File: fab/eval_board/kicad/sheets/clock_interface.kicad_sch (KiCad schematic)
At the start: 17 parts, among them J10 SMA_RF4, J2 USB-C, J5 JTAG_2x5, J6 GPIO_2x7, J7 SMA_RF1, J8 SMA_RF2, J9 SMA_RF3, SW1 RESET, U20 Si5395A, U22 FT232H, U23 W25Q128JVS, Y1 100MHz_TCXO

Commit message: fix: regenerate KiCad files in valid KiCad 8 format
- Rewrote all .kicad_sch files with proper lib_symbols sections,
  symbol instances, wires, hierarchical sheet references, and
  power port definitions (removed invalid ';;' comment syntax)
- Fixed .kicad_pcb: removed comment lines, added 922 missing net
  definitions, fixed gr_text justify format
- Regenerated Gerbers from fixed PCB using kicad-cli (30 files)
- All files validated with kicad-cli: schematic exports 5-page PDF,
  PCB exports SVG, DRC/ERC both run without parse errors
- Added regenerate_kicad.py generator script for reproducibility

Co-Authored-By: Bola Olatunji <bola.olatunji@ai.lightos.sh>
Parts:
- removed D1: LED_Green_PWR, LED_SMD:LED_0603_1608Metric, symbol Device:LED
- removed D2: LED_Blue_ACT, LED_SMD:LED_0603_1608Metric, symbol Device:LED
- removed D3: LED_Red_FAULT, LED_SMD:LED_0603_1608Metric, symbol Device:LED
- removed D4: LED_Yellow_LINK, LED_SMD:LED_0603_1608Metric, symbol Device:LED
- removed D5: PRTR5V0U2X, Package_TO_SOT_SMD:SOD-323, symbol Diode:PRTR5V0U2X
- removed J10: SMA_RF4, Connector_Coaxial:SMA_Amphenol_132134-11_Vertical, symbol Connector:Conn_Coaxial
- removed J2: USB-C, Connector_USB:USB_C_Receptacle_GCT_USB4110-GF-A, symbol Connector:USB_C_Receptacle_USB2.0
- removed J5: JTAG_2x5, Connector_PinHeader_1.27mm:PinHeader_2x05_P1.27mm_Vertical, symbol Connector:Conn_ARM_JTAG_SWD_10
- removed J6: GPIO_2x7, Connector_PinHeader_1.27mm:PinHeader_2x07_P1.27mm_Vertical, symbol Connector_Generic:Conn_02x07_Odd_Even
- removed J7: SMA_RF1, Connector_Coaxial:SMA_Amphenol_132134-11_Vertical, symbol Connector:Conn_Coaxial
- removed J8: SMA_RF2, Connector_Coaxial:SMA_Amphenol_132134-11_Vertical, symbol Connector:Conn_Coaxial
- removed J9: SMA_RF3, Connector_Coaxial:SMA_Amphenol_132134-11_Vertical, symbol Connector:Conn_Coaxial
- removed U23: W25Q128JVS, Package_SON:WSON-8-1EP_2x3mm_P0.5mm, symbol Memory_Flash:W25Q128JVS
- removed Y1: 100MHz_TCXO, Oscillator:Oscillator_SMD_3225-4Pin_3.2x2.5mm, symbol Oscillator:SiT5356
- added C50, C51, C52, C53: 100nF, Capacitor_SMD:C_0402_1005Metric, symbol Device:C
- added J2: USB_C, Connector_USB:USB_C_Receptacle_GCT_USB4105-xx-A_16P_TopMnt_Horizontal, symbol Connector:USB_C_Receptacle
- added J6: GPIO_2x7, Connector_PinHeader_2.54mm:PinHeader_2x07_P2.54mm_Vertical, symbol Connector_Generic:Conn_02x07
- added Y1: 100MHz_TCXO, Crystal:Crystal_SMD_2520-4Pin_2.5x2.0mm, symbol Device:Crystal
- SW1: footprint Button_Switch_SMD:SW_Push_1P1T_NO_CK_KSC701J -> Button_Switch_SMD:SW_Push_1P1T_NO_CK_KSC7xxJ; MPN B3F-1000 -> KSC721J
- U20: footprint LightRail:QFN-28_5x5mm -> Package_DFN_QFN:QFN-44-1EP_7x7mm_P0.5mm_EP5.15x5.15mm; MPN Si5395A-A-GM -> SI5395A-A-GM
- U22: value FT232H -> FT232HL; footprint Package_DFN_QFN:QFN-48-1EP_7x7mm_P0.5mm_EP5.15x5.15mm -> Package_QFP:LQFP-48_7x7mm_P0.5mm; MPN FT232HQ -> FT232HL-REEL
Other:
- title: Clock & Test Interface — LightRail Eval Board -> Clock Generation + Test Interface - LightRail Eval Board

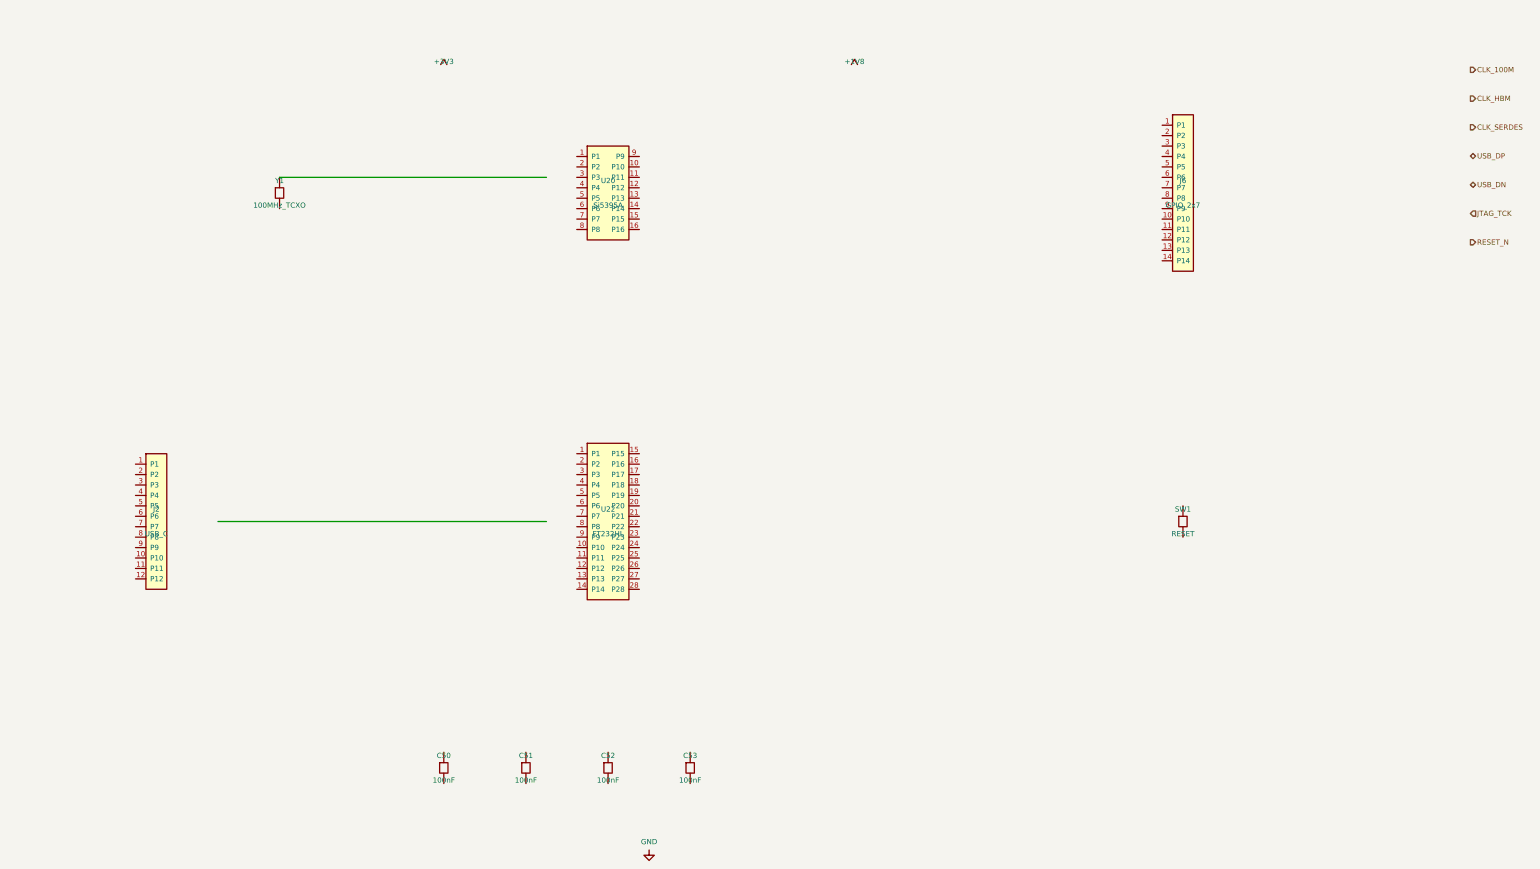
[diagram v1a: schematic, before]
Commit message: refactor: improve ERC quality via grid snapping and power flags
Co-Authored-By: Bola Olatunji <bola.olatunji@ai.lightos.sh>
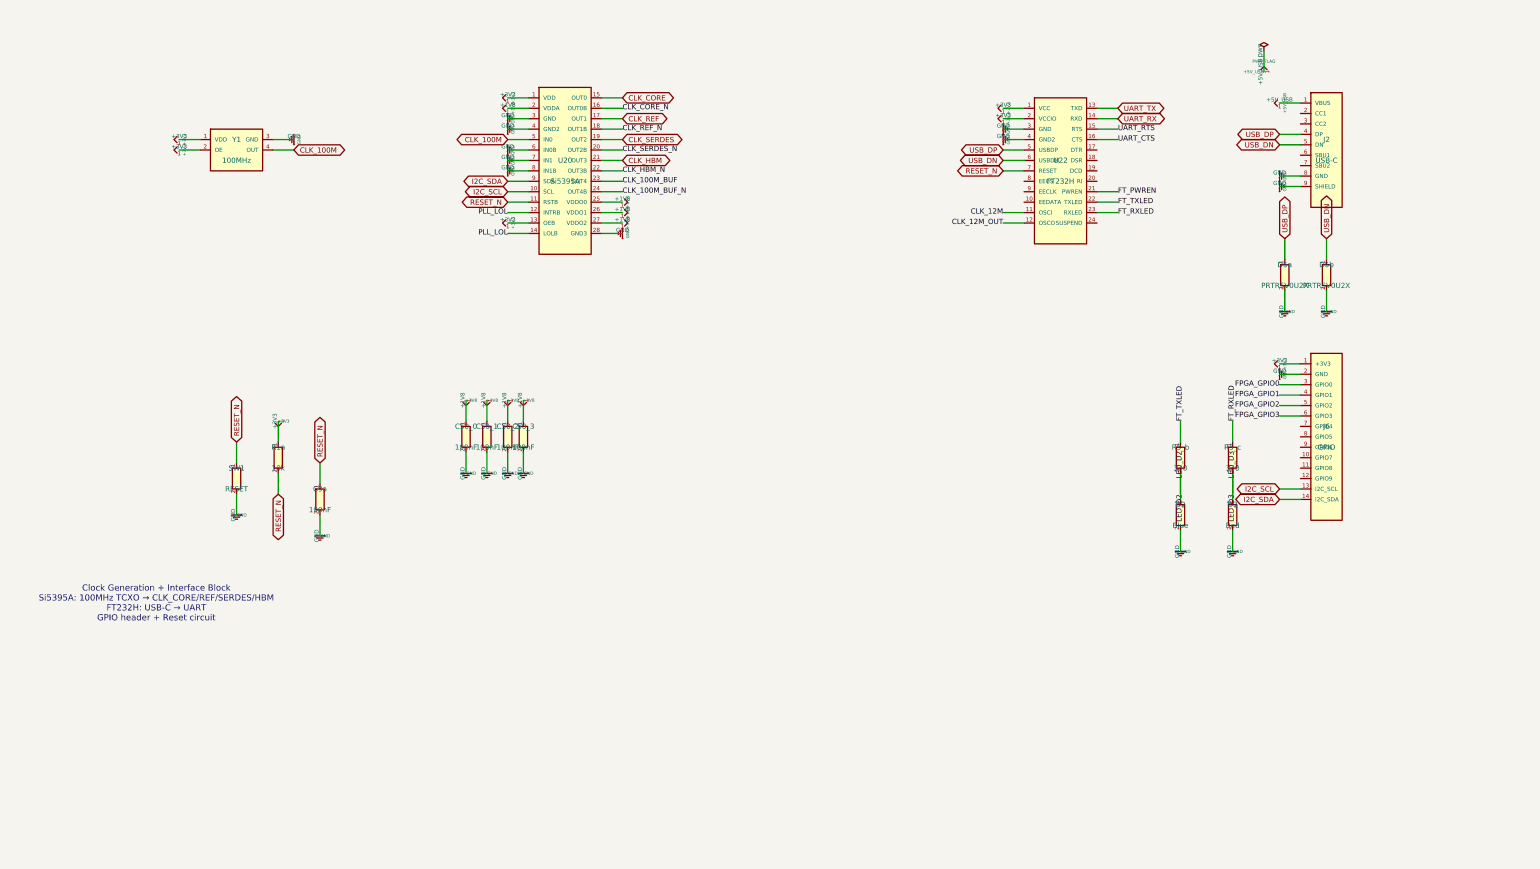
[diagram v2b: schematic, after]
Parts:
- removed C50, C51, C52, C53: 100nF, Capacitor_SMD:C_0402_1005Metric, symbol Device:C
- removed J2: USB_C, Connector_USB:USB_C_Receptacle_GCT_USB4105-xx-A_16P_TopMnt_Horizontal, symbol Connector:USB_C_Receptacle
- removed J6: GPIO_2x7, Connector_PinHeader_2.54mm:PinHeader_2x07_P2.54mm_Vertical, symbol Connector_Generic:Conn_02x07
- removed Y1: 100MHz_TCXO, Crystal:Crystal_SMD_2520-4Pin_2.5x2.0mm, symbol Device:Crystal
- added C50_0, C50_1, C50_2, C50_3: 100nF, symbol Device:C
- added C9a: 100nF, Capacitor_SMD:C_0402, symbol Device:C
- added D2: Blue, LED_SMD:LED_0603, symbol Device:LED
- added D3: Red, LED_SMD:LED_0603, symbol Device:LED
- added D5a, D5b: PRTR5V0U2X, Package_SOD:SOD-323, symbol Device:D_TVS
- added J2: USB-C, Connector_USB:USB_C_Receptacle_GCT_USB4110, symbol Connector:USB_C_16Pin
- added J6: GPIO, Connector_PinHeader_1.27mm:PinHeader_2x07_P1.27mm_Vertical, symbol Connector:PinHeader_2x07
- added R1a: 10k, Resistor_SMD:R_0402, symbol Device:R
- added R5_b, R5_c: 330, Resistor_SMD:R_0402, symbol Device:R
- added Y1: 100MHz, Crystal:Crystal_SMD_3215-4Pin, symbol Device:Crystal_4Pin
- SW1: footprint Button_Switch_SMD:SW_Push_1P1T_NO_CK_KSC7xxJ -> Button_Switch_SMD:Tactile_4.5x4.5mm; MPN KSC721J -> B3F-1000
- U20: footprint Package_DFN_QFN:QFN-44-1EP_7x7mm_P0.5mm_EP5.15x5.15mm -> Package_DFN_QFN:QFN-28_5x5mm; MPN SI5395A-A-GM -> Si5395A-A-GM
- U22: value FT232HL -> FT232H; footprint Package_QFP:LQFP-48_7x7mm_P0.5mm -> Package_DFN_QFN:QFN-48_7x7mm; MPN FT232HL-REEL -> FT232HQ
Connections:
- net +1V8: now also U20.2 (VDDA), U20.25 (VDDO0), U20.26 (VDDO1), U20.27 (VDDO2), C50_0.1, C50_1.1, C50_2.1, C50_3.1
- net +3V3: now also U20.1 (VDD), U20.13 (OEB), U22.1 (VCC), U22.2 (VCCIO), J6.1 (+3V3), R1a.1, Y1.1 (VDD), Y1.2 (OE)
- net CLK_100M: now also U20.5 (IN0), Y1.4 (OUT)
- net CLK_HBM: now also U20.21 (OUT3)
- net CLK_SERDES: now also U20.19 (OUT2)
- net GND: now also SW1.2, U20.28 (GND3), U20.3 (GND), U20.4 (GND2), U20.6 (IN0B), U20.7 (IN1), U20.8 (IN1B), U22.3 (GND), U22.4 (GND2), C50_0.2, C50_1.2, C50_2.2, C50_3.2, C9a.2, D2.2, D3.2, D5a.2, D5b.2, J2.8 (GND), J2.9 (SHIELD), J6.2 (GND), Y1.3 (GND)
- net RESET_N: now also SW1.1, U20.11 (RSTB), U22.7 (RESET), C9a.1, R1a.2
- net USB_DN: now also U22.6 (USBDM), D5b.1, J2.5 (DN)
- net USB_DP: now also U22.5 (USBDP), D5a.1, J2.4 (DP)
- net CLK_12M: now reaches U22.11 (OSCI)
- net CLK_12M_OUT: now reaches U22.12 (OSCO)
- net UART_TX: now reaches U22.13 (TXD)
- net UART_RX: now reaches U22.14 (RXD)
- net UART_RTS: now reaches U22.15 (RTS)
- net UART_CTS: now reaches U22.16 (CTS)
- net FT_PWREN: now reaches U22.21 (PWREN)
- net FT_TXLED: now reaches U22.22 (TXLED)
- net FT_TXLED: now also R5_b.1
- net FT_RXLED: now reaches U22.23 (RXLED)
- net FT_RXLED: now also R5_c.1
- net I2C_SCL: now reaches U20.10 (SCL)
- net I2C_SCL: now also J6.13 (I2C_SCL)
- net PLL_LOL: now reaches U20.12 (INTRB)
- net PLL_LOL: now also U20.14 (LOLB)
- net CLK_CORE: now reaches U20.15 (OUT0)
- net CLK_CORE_N: now reaches U20.16 (OUT0B)
- net I2C_SDA: now reaches U20.9 (SDA)
- net I2C_SDA: now also J6.14 (I2C_SDA)
- new net +5V_USB: J2.1 (VBUS)
- new net CLK_100M_BUF: U20.23 (OUT4)
- new net CLK_100M_BUF_N: U20.24 (OUT4B)
- new net CLK_HBM_N: U20.22 (OUT3B)
- new net CLK_REF: U20.17 (OUT1)
- new net CLK_REF_N: U20.18 (OUT1B)
- new net CLK_SERDES_N: U20.20 (OUT2B)
- new net FPGA_GPIO0: J6.3 (GPIO0)
- new net FPGA_GPIO1: J6.4 (GPIO1)
- new net FPGA_GPIO2: J6.5 (GPIO2)
- new net FPGA_GPIO3: J6.6 (GPIO3)
- new net LED_D2: D2.1, R5_b.2
- new net LED_D3: D3.1, R5_c.2
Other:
- note added: "Clock Generation + Interface Block Si5395A: 100MHz TCXO → CLK_CORE/REF/SERDES/HBM FT232H: USB-C → UART GPIO header + Reset circuit"
- title: Clock Generation + Test Interface - LightRail Eval Board -> Clock + Interface - LightRail Eval Board
